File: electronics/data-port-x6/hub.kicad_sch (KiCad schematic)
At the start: 54 parts, among them J1 LEAD, Q1 2N7002, Q2 2N7002, Q3 2N7002, U1 USB2517I-JZX, U2 TCA9535RTWR, U3 AP2114H-3.3TRG1, U4 H5VU25UC, U5 MAX809S, U6 TCA9535RTWR, Y1 X322524MSB4SI

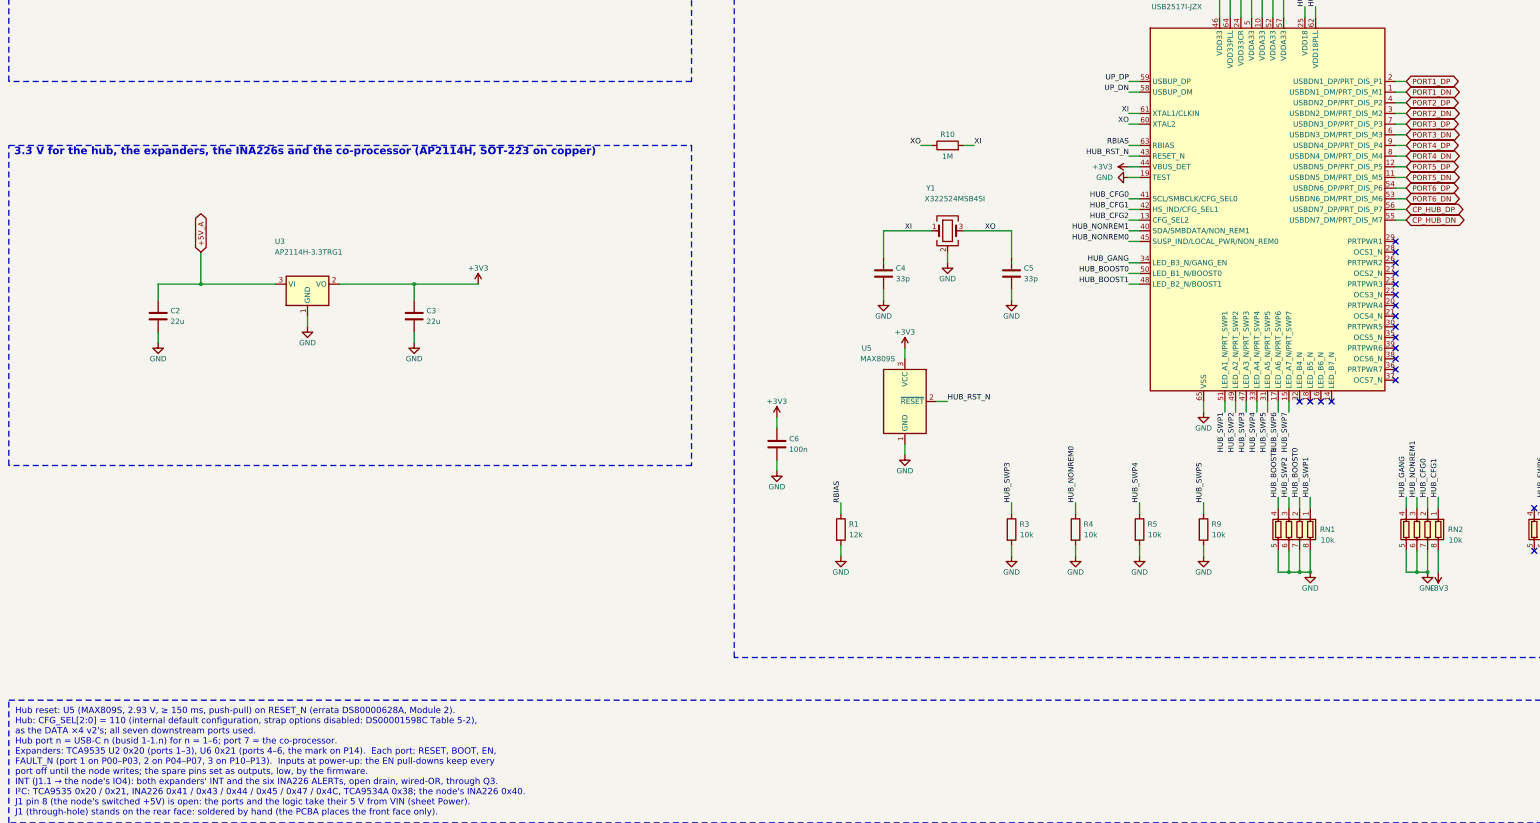
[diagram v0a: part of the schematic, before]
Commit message: DATA x6: placement, the functions grouped as the study drew them
The board placed, not routed (DRC: only the unrouted links; ERC 0).  Bands, top to bottom:
- the co-processor (the v2's block, 31.1 mm west) and its SWD header under it; the six
  colour blocks (z 65-81); the hub (the v2's block, a row lower) with converter B
  (+5V_B, the top-right corner) over it;
- per port its pin chain right under its block (the H5VU25UC, the 100 ohm arrays, the
  LSF0108, two rows of 0402);
- converter A (+5V_A) west, the three crosspoints with a TCA9535 between two, J1 east with
  the lead's ESD and the I2C isolation beside it; the matrix expander (TCA9534A) and the
  -5 V inverter under the SWD header, by the co-processor;
- a corridor for the USB pairs, then each port's switch and current sense, then its VBUS
  22 uF, CC resistors and LED over the receptacle, the USBLC6 in the gap west of it (port
  1's over its receptacle: the cradle's band beside it).
- VIN's 33 uF and J3 (rear face) under the blocks' legend; the 3.3 V LDO under converter A.

The hub's south face DN1-5 now feeds USB-C 2-6 and its west face DN6 USB-C 1, so the pairs
come down and turn west in lanes, the lowest dropping off first, none crossing (DN7: the
co-processor).  The power plane: +3V3 over the clusters' split (y 64.6), +5V_A / +5V_B
under it either side of x 50, each fed from its converter down the cradle's band at its
end; no B.Cu track crosses the main splits.  Rear-face test points spaced so their names
do not overlap; each port number over its block.

Co-Authored-By: Claude Opus 5.5 <noreply@anthropic.com>
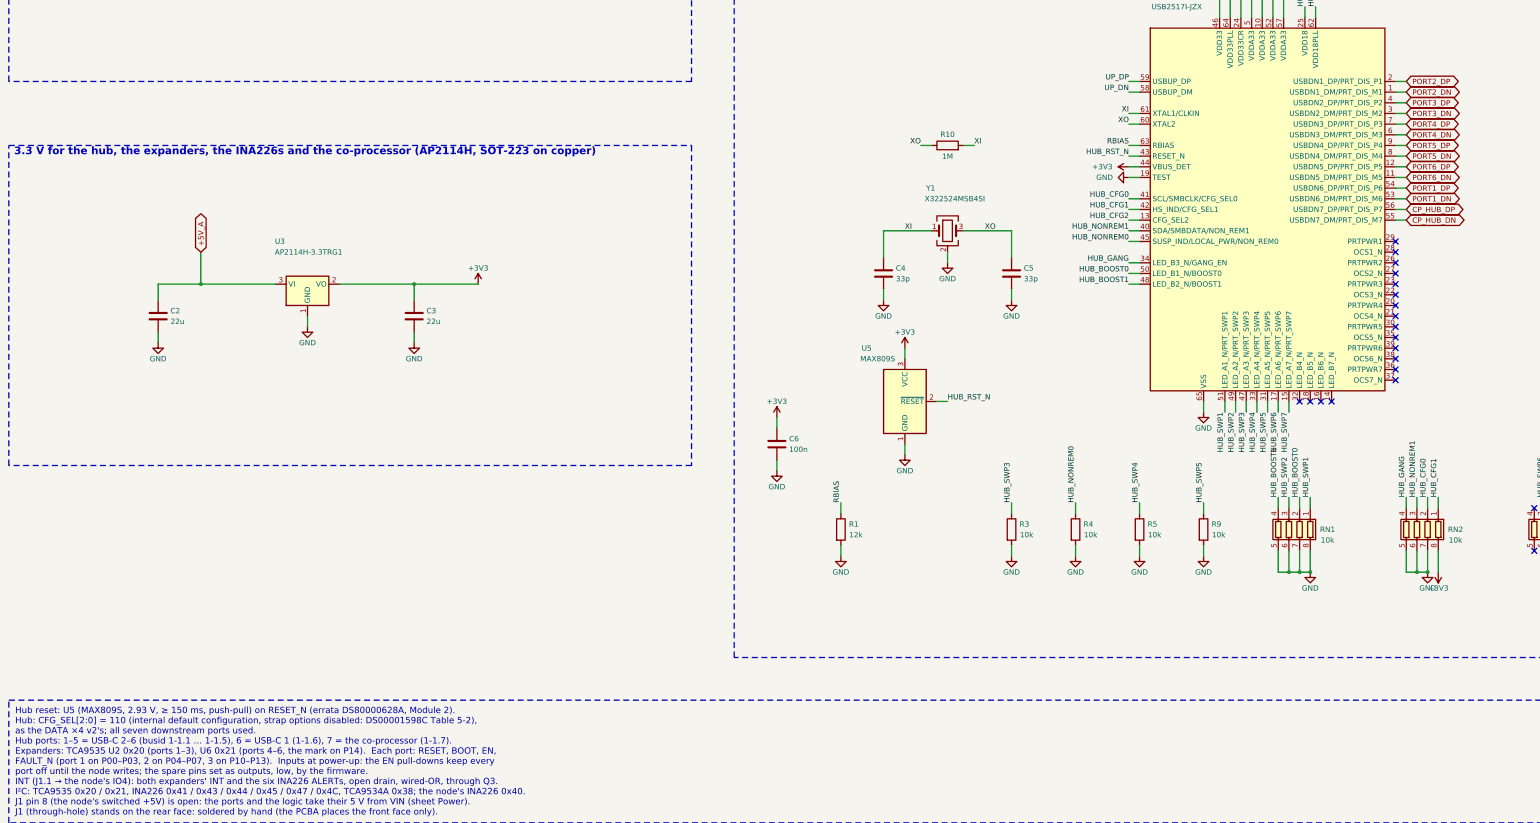
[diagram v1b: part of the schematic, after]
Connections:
- net PORT1_DN: now also U1.53 (USBDN6_DM/PRT_DIS_M6); no longer U1.1 (USBDN1_DM/PRT_DIS_M1)
- net PORT1_DP: now also U1.54 (USBDN6_DP/PRT_DIS_P6); no longer U1.2 (USBDN1_DP/PRT_DIS_P1)
- net PORT2_DN: now also U1.1 (USBDN1_DM/PRT_DIS_M1); no longer U1.3 (USBDN2_DM/PRT_DIS_M2)
- net PORT2_DP: now also U1.2 (USBDN1_DP/PRT_DIS_P1); no longer U1.4 (USBDN2_DP/PRT_DIS_P2)
- net PORT3_DN: now also U1.3 (USBDN2_DM/PRT_DIS_M2); no longer U1.6 (USBDN3_DM/PRT_DIS_M3)
- net PORT3_DP: now also U1.4 (USBDN2_DP/PRT_DIS_P2); no longer U1.7 (USBDN3_DP/PRT_DIS_P3)
- net PORT4_DN: now also U1.6 (USBDN3_DM/PRT_DIS_M3); no longer U1.8 (USBDN4_DM/PRT_DIS_M4)
- net PORT4_DP: now also U1.7 (USBDN3_DP/PRT_DIS_P3); no longer U1.9 (USBDN4_DP/PRT_DIS_P4)
- net PORT5_DN: now also U1.8 (USBDN4_DM/PRT_DIS_M4); no longer U1.11 (USBDN5_DM/PRT_DIS_M5)
- net PORT5_DP: now also U1.9 (USBDN4_DP/PRT_DIS_P4); no longer U1.12 (USBDN5_DP/PRT_DIS_P5)
- net PORT6_DN: now also U1.11 (USBDN5_DM/PRT_DIS_M5); no longer U1.53 (USBDN6_DM/PRT_DIS_M6)
- net PORT6_DP: now also U1.12 (USBDN5_DP/PRT_DIS_P5); no longer U1.54 (USBDN6_DP/PRT_DIS_P6)
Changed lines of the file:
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@@
 		)
 	)
-	(global_label "PORT1_DP"
+	(global_label "PORT2_DP"
 		(shape bidirectional)
 		(at 347.98 127 0)
@@
 		)
 	)
-	(global_label "PORT1_DN"
+	(global_label "PORT2_DN"
 		(shape bidirectional)
 		(at 347.98 129.54 0)
@@
 		)
 	)
-	(global_label "PORT2_DP"
+	(global_label "PORT3_DP"
 		(shape bidirectional)
 		(at 347.98 132.08 0)
@@
 		)
 	)
-	(global_label "PORT2_DN"
+	(global_label "PORT3_DN"
 		(shape bidirectional)
 		(at 347.98 134.62 0)
@@
 		)
 	)
-	(global_label "PORT3_DP"
+	(global_label "PORT4_DP"
 		(shape bidirectional)
 		(at 347.98 137.16 0)
@@
 		)
 	)
-	(global_label "PORT3_DN"
+	(global_label "PORT4_DN"
 		(shape bidirectional)
 		(at 347.98 139.7 0)
@@
 		)
 	)
-	(global_label "PORT4_DP"
+	(global_label "PORT5_DP"
 		(shape bidirectional)
 		(at 347.98 142.24 0)
@@
 		)
 	)
-	(global_label "PORT4_DN"
+	(global_label "PORT5_DN"
 		(shape bidirectional)
 		(at 347.98 144.78 0)
@@
 		)
 	)
-	(global_label "PORT5_DP"
+	(global_label "PORT6_DP"
 		(shape bidirectional)
 		(at 347.98 147.32 0)
@@
 		)
 	)
-	(global_label "PORT5_DN"
+	(global_label "PORT6_DN"
 		(shape bidirectional)
 		(at 347.98 149.86 0)
@@
 		)
 	)
-	(global_label "PORT6_DP"
+	(global_label "PORT1_DP"
 		(shape bidirectional)
 		(at 347.98 152.4 0)
@@
 		)
 	)
-	(global_label "PORT6_DN"
+	(global_label "PORT1_DN"
 		(shape bidirectional)
 		(at 347.98 154.94 0)
@@
 		)
 	)
-	(text_box "Hub reset: U5 (MAX809S, 2.93 V, ≥ 150 ms, push-pull) on RESET_N (errata DS80000628A, Module 2).\nHub: CFG_SEL[2:0] = 110 (internal default configuration, strap options disabled: DS00001598C Table 5-2),\n  as the DATA ×4 v2's; all seven downstream ports used.\nHub port n = USB-C n (busid 1-1.n) for n = 1–6; port 7 = the co-processor.\nExpanders: TCA9535 U2 0x20 (ports 1–3), U6 0x21 (ports 4–6, the mark on P14).  Each port: RESET, BOOT, EN,\n  FAULT_N (port 1 on P00–P03, 2 on P04–P07, 3 on P10–P13).  Inputs at power-up: the EN pull-downs keep every\n  port off until the node writes; the spare pins set as outputs, low, by the firmware.\nINT (J1.1 → the node's IO4): both expanders' INT and the six INA226 ALERTs, open drain, wired-OR, through Q3.\nI²C: TCA9535 0x20 / 0x21, INA226 0x41 / 0x43 / 0x44 / 0x45 / 0x47 / 0x4C, TCA9534A 0x38; the node's INA226 0x40.\nJ1 pin 8 (the node's switched +5V) is open: the ports and the logic take their 5 V from VIN (sheet Power).\nJ1 (through-hole) stands on the rear face: soldered by hand (the PCBA places the front face only)."
+	(text_box "Hub reset: U5 (MAX809S, 2.93 V, ≥ 150 ms, push-pull) on RESET_N (errata DS80000628A, Module 2).\nHub: CFG_SEL[2:0] = 110 (internal default configuration, strap options disabled: DS00001598C Table 5-2),\n  as the DATA ×4 v2's; all seven downstream ports used.\nHub ports: 1–5 = USB-C 2–6 (busid 1-1.1 … 1-1.5), 6 = USB-C 1 (1-1.6), 7 = the co-processor (1-1.7).\nExpanders: TCA9535 U2 0x20 (ports 1–3), U6 0x21 (ports 4–6, the mark on P14).  Each port: RESET, BOOT, EN,\n  FAULT_N (port 1 on P00–P03, 2 on P04–P07, 3 on P10–P13).  Inputs at power-up: the EN pull-downs keep every\n  port off until the node writes; the spare pins set as outputs, low, by the firmware.\nINT (J1.1 → the node's IO4): both expanders' INT and the six INA226 ALERTs, open drain, wired-OR, through Q3.\nI²C: TCA9535 0x20 / 0x21, INA226 0x41 / 0x43 / 0x44 / 0x45 / 0x47 / 0x4C, TCA9534A 0x38; the node's INA226 0x40.\nJ1 pin 8 (the node's switched +5V) is open: the ports and the logic take their 5 V from VIN (sheet Power).\nJ1 (through-hole) stands on the rear face: soldered by hand (the PCBA places the front face only)."
 		(exclude_from_sim no)
 		(at 15.24 274.32 0)
